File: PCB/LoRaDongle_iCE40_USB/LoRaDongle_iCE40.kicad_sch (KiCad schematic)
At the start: 6 parts, among them J1 USB_A, J2 Conn_01x08

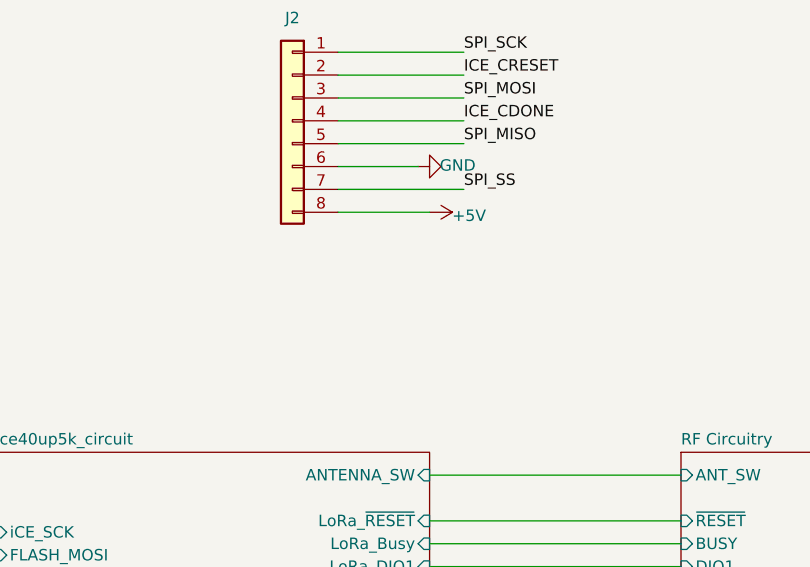
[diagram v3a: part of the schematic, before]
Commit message: updated schematic to QFN ice40
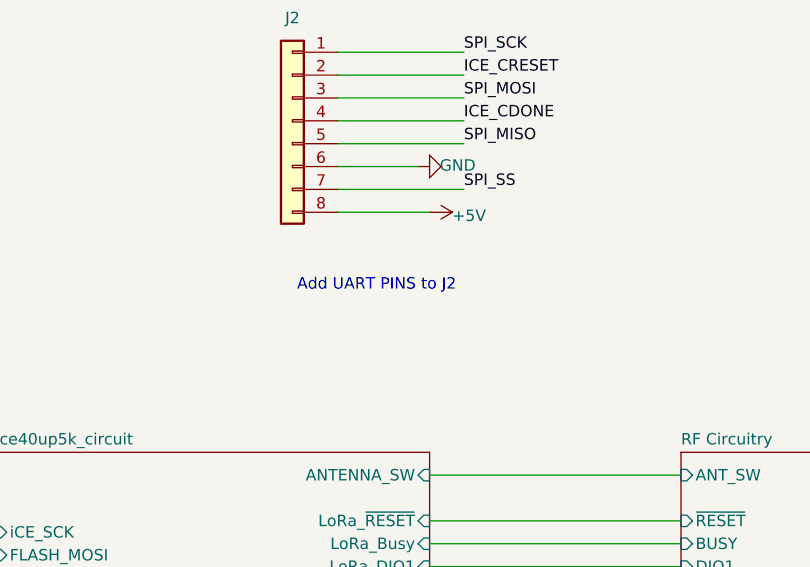
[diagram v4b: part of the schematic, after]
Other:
- note added: "Add UART PINS to J2"
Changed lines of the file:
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@@
     (stroke (width 0) (type default) (color 0 0 0 0))
+  )
+  (text "Add UART PINS to J2" (at 156.718 66.04 0)
+    (effects (font (size 1.27 1.27)) (justify left bottom))
   )
   (text "Configuration Header/Testpoints" (at 149.86 31.75 0)
@@
       (reference "#PWR017") (unit 1) (value "GND") (footprint "")
     )
-    (path "/00000000-0000-0000-0000-0000618d30e5/00000000-0000-0000-0000-000061b1a37c"
-      (reference "#PWR018") (unit 1) (value "GND") (footprint "")
-    )
     (path "/00000000-0000-0000-0000-0000618d30e5/00000000-0000-0000-0000-000061bb6e8b"
       (reference "#PWR019") (unit 1) (value "GND") (footprint "")
@@
       (reference "C55") (unit 1) (value "1uF") (footprint "Capacitor_SMD:C_0402_1005Metric_Pad0.74x0.62mm_HandSolder")
     )
+    (path "/00000000-0000-0000-0000-0000618d30e5/46466808-c3e7-4f98-9aec-1d0c34898718"
+      (reference "C?") (unit 1) (value "100nF") (footprint "Capacitor_SMD:C_0402_1005Metric_Pad0.74x0.62mm_HandSolder")
+    )
+    (path "/00000000-0000-0000-0000-0000618d30e5/798270cd-5a11-4361-915d-f990179c4c4d"
+      (reference "C?") (unit 1) (value "1uF") (footprint "Capacitor_SMD:C_0402_1005Metric_Pad0.74x0.62mm_HandSolder")
+    )
     (path "/00000000-0000-0000-0000-0000614f0720/00000000-0000-0000-0000-000061d45a7d"
       (reference "CTL2") (unit 1) (value "CTL2") (footprint "TestPoint:TestPoint_Pad_D2.5mm")
@@
       (reference "IC1") (unit 1) (value "93LC56BT-I_OT") (footprint "93LC56B-I_OT_KiCad:SOT95P270X145-6N")
     )
-    (path "/00000000-0000-0000-0000-0000618d30e5/00000000-0000-0000-0000-000061af95e0"
-      (reference "IC2") (unit 1) (value "ICE40UP5K-UWG30ITR1K") (footprint "ICE40UP5K-UWG30ITR1K_KiCad:BGA30C40P5X6_211X254X60")
-    )
     (path "/00000000-0000-0000-0000-0000618d30e5/f356286c-5381-4e19-bb6f-5643e839da16"
       (reference "IC3") (unit 1) (value "SGP40-D-R4") (footprint "KiCad_SGP40-D-R4:SON80P244X244X95-7N")
@@
       (reference "J8") (unit 1) (value "Jumper_2_Open") (footprint "Connector_PinHeader_2.54mm:PinHeader_1x02_P2.54mm_Vertical")
     )
+    (path "/00000000-0000-0000-0000-0000618d30e5/ce712167-16e9-4787-a679-59dd7042cff8"
+      (reference "J9") (unit 1) (value "Conn_01x17_Male") (footprint "Connector_PinHeader_2.54mm:PinHeader_1x17_P2.54mm_Vertical")
+    )
     (path "/00000000-0000-0000-0000-0000618d30e5/671729c9-90fa-4cb2-ac5f-b42b2914af94"
       (reference "JP1") (unit 1) (value "SolderJumper_2_Open") (footprint "Resistor_SMD:R_0603_1608Metric_Pad0.98x0.95mm_HandSolder")
@@
       (reference "U5") (unit 1) (value "W25Q128JVS") (footprint "Package_SO:SOIC-8_5.23x5.23mm_P1.27mm")
     )
+    (path "/00000000-0000-0000-0000-0000618d30e5/1ce0333e-6de8-4616-940b-d476ef4ba385"
+      (reference "U6") (unit 1) (value "ICE40UP5K-SG48ITR") (footprint "Package_DFN_QFN:QFN-48-1EP_7x7mm_P0.5mm_EP5.6x5.6mm")
+    )
+    (path "/00000000-0000-0000-0000-0000618d30e5/4ca096aa-df1d-4e7c-9158-2031ee071920"
+      (reference "U6") (unit 2) (value "ICE40UP5K-SG48ITR") (footprint "Package_DFN_QFN:QFN-48-1EP_7x7mm_P0.5mm_EP5.6x5.6mm")
+    )
+    (path "/00000000-0000-0000-0000-0000618d30e5/aec76c06-f2a1-41fa-89c1-1f27b85458b6"
+      (reference "U6") (unit 3) (value "ICE40UP5K-SG48ITR") (footprint "Package_DFN_QFN:QFN-48-1EP_7x7mm_P0.5mm_EP5.6x5.6mm")
+    )
+    (path "/00000000-0000-0000-0000-0000618d30e5/53fb07c9-cb96-4429-a71b-a426d6ac2c63"
+      (reference "U6") (unit 4) (value "ICE40UP5K-SG48ITR") (footprint "Package_DFN_QFN:QFN-48-1EP_7x7mm_P0.5mm_EP5.6x5.6mm")
+    )
     (path "/00000000-0000-0000-0000-0000618d30e5/00000000-0000-0000-0000-000061bb2826"

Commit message: updated routing
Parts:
- removed J2: Conn_01x08, Connector_PinHeader_2.54mm:PinHeader_2x04_P2.54mm_Vertical, symbol Connector_Generic:Conn_01x08
- added J2: Conn_01x10_Male, Connector_PinHeader_2.54mm:PinHeader_2x05_P2.54mm_Vertical, symbol Connector:Conn_01x10_Male
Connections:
- net +5V: now also J2.10 (Pin_10)
- net GND: now also J2.9 (Pin_9)
- net ICE_CDONE: now also J2.4 (Pin_4)
- net ICE_CRESET: now also J2.2 (Pin_2)
- net SPI_MISO: now also J2.5 (Pin_5)
- net SPI_MOSI: now also J2.3 (Pin_3)
- net SPI_SCK: now also J2.1 (Pin_1)
- net SPI_SS: now also J2.6 (Pin_6)
- new net UART_RX: J2.7 (Pin_7)
- new net UART_TX: J2.8 (Pin_8)
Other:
- note removed: "Add UART PINS to J2"
- note removed: "Configuration Header/Testpoints"

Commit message: routing complete
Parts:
- added 5V1: 5V, TestPoint:TestPoint_Pad_D2.5mm, symbol Connector:TestPoint_Flag
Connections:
- net +5V: now also 5V1.1
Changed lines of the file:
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@@
   (junction (at 39.37 92.71) (diameter 0) (color 0 0 0 0)
+  )
+  (junction (at 112.014 40.64) (diameter 0) (color 0 0 0 0)
   )
   (no_connect (at 27.94 107.95))
@@
     (stroke (width 0) (type default) (color 0 0 0 0))
   )
-  (wire (pts (xy 112.014 37.338) (xy 112.014 44.958))
+  (wire (pts (xy 112.014 37.338) (xy 112.014 40.64))
     (stroke (width 0) (type default) (color 0 0 0 0))
   )
@@
   )
   (wire (pts (xy 30.48 107.95) (xy 30.48 110.49))
+    (stroke (width 0) (type default) (color 0 0 0 0))
+  )
+  (wire (pts (xy 112.014 40.64) (xy 112.014 44.958))
     (stroke (width 0) (type default) (color 0 0 0 0))
   )
@@
     )
     (property "Datasheet" "" (id 3) (at 155.956 59.436 0)
+      (effects (font (size 1.27 1.27)) hide)
+    )
+    (pin "1")
+  )
+  (symbol (lib_id "Connector:TestPoint_Flag") (at 112.014 40.64 0) (unit 1)
+    (in_bom yes) (on_board yes)
+    (property "Reference" "5V1" (id 0) (at 119.761 39.4208 0))
+    (property "Value" "5V" (id 1) (at 119.7864 39.4208 90)
+      (effects (font (size 1.27 1.27)) hide)
+    )
+    (property "Footprint" "TestPoint:TestPoint_Pad_D2.5mm" (id 2) (at 117.094 40.64 0)
+      (effects (font (size 1.27 1.27)) hide)
+    )
+    (property "Datasheet" "~" (id 3) (at 117.094 40.64 0)
+      (effects (font (size 1.27 1.27)) hide)
+    )
+    (property "Description" "Test Point" (id 4) (at 112.014 40.64 0)
+      (effects (font (size 1.27 1.27)) hide)
+    )
+    (property "Manufacturer" "-" (id 5) (at 112.014 40.64 0)
+      (effects (font (size 1.27 1.27)) hide)
+    )
+    (property "Manufacturer Part Number" "-" (id 6) (at 112.014 40.64 0)
+      (effects (font (size 1.27 1.27)) hide)
+    )
+    (property "Package" "-" (id 7) (at 112.014 40.64 0)
+      (effects (font (size 1.27 1.27)) hide)
+    )
+    (property "Type" "-" (id 8) (at 112.014 40.64 0)
       (effects (font (size 1.27 1.27)) hide)
     )
@@
       (reference "3V3") (unit 1) (value "3.3V") (footprint "TestPoint:TestPoint_Pad_D2.5mm")
     )
+    (path "/5fa5f0aa-6f4c-4b09-ab26-5eb3ebef5de0"
+      (reference "5V1") (unit 1) (value "5V") (footprint "TestPoint:TestPoint_Pad_D2.5mm")
+    )
     (path "/00000000-0000-0000-0000-000061593dc4"

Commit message: updated BOM
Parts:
- J2: Manufacturer (none) -> -; Manufacturer Part Number (none) -> -; Package (none) -> -
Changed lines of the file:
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@@
+      (effects (font (size 1.27 1.27)) hide)
+    )
+    (property "Description" "2x05 Male Header" (id 4) (at 147.828 49.276 0)
+      (effects (font (size 1.27 1.27)) hide)
+    )
+    (property "Manufacturer" "-" (id 5) (at 147.828 49.276 0)
+      (effects (font (size 1.27 1.27)) hide)
+    )
+    (property "Manufacturer Part Number" "-" (id 6) (at 147.828 49.276 0)
+      (effects (font (size 1.27 1.27)) hide)
+    )
+    (property "Package" "-" (id 7) (at 147.828 49.276 0)
       (effects (font (size 1.27 1.27)) hide)
     )

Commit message: updated silkscreen
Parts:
- J2: Type (none) -> Through HOle
- R1, R2: Type (none) -> SMD
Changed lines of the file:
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@@
+      (effects (font (size 1.27 1.27)) hide)
+    )
+    (property "Type" "SMD" (id 8) (at 50.8 97.79 0)
       (effects (font (size 1.27 1.27)) hide)
     )
@@
       (effects (font (size 1.27 1.27)) hide)
     )
+    (property "Type" "SMD" (id 8) (at 50.8 100.33 0)
+      (effects (font (size 1.27 1.27)) hide)
+    )
     (pin "1")
     (pin "2")
@@
     )
     (property "Package" "-" (id 7) (at 147.828 49.276 0)
+      (effects (font (size 1.27 1.27)) hide)
+    )
+    (property "Type" "Through HOle" (id 8) (at 147.828 49.276 0)
       (effects (font (size 1.27 1.27)) hide)
     )
@@
     )
     (path "/00000000-0000-0000-0000-0000618d30e5/1ce0333e-6de8-4616-940b-d476ef4ba385"
-      (reference "U6") (unit 1) (value "ICE40UP5K-SG48ITR") (footprint "Package_DFN_QFN:QFN-48-1EP_7x7mm_P0.5mm_EP5.6x5.6mm")
+      (reference "U6") (unit 1) (value "ICE40UP5K-SG48I") (footprint "Package_DFN_QFN:QFN-48-1EP_7x7mm_P0.5mm_EP5.6x5.6mm")
     )
     (path "/00000000-0000-0000-0000-0000618d30e5/4ca096aa-df1d-4e7c-9158-2031ee071920"
-      (reference "U6") (unit 2) (value "ICE40UP5K-SG48ITR") (footprint "Package_DFN_QFN:QFN-48-1EP_7x7mm_P0.5mm_EP5.6x5.6mm")
+      (reference "U6") (unit 2) (value "ICE40UP5K-SG48I") (footprint "Package_DFN_QFN:QFN-48-1EP_7x7mm_P0.5mm_EP5.6x5.6mm")
     )
     (path "/00000000-0000-0000-0000-0000618d30e5/aec76c06-f2a1-41fa-89c1-1f27b85458b6"
-      (reference "U6") (unit 3) (value "ICE40UP5K-SG48ITR") (footprint "Package_DFN_QFN:QFN-48-1EP_7x7mm_P0.5mm_EP5.6x5.6mm")
+      (reference "U6") (unit 3) (value "ICE40UP5K-SG48I") (footprint "Package_DFN_QFN:QFN-48-1EP_7x7mm_P0.5mm_EP5.6x5.6mm")
     )
     (path "/00000000-0000-0000-0000-0000618d30e5/53fb07c9-cb96-4429-a71b-a426d6ac2c63"
-      (reference "U6") (unit 4) (value "ICE40UP5K-SG48ITR") (footprint "Package_DFN_QFN:QFN-48-1EP_7x7mm_P0.5mm_EP5.6x5.6mm")
+      (reference "U6") (unit 4) (value "ICE40UP5K-SG48I") (footprint "Package_DFN_QFN:QFN-48-1EP_7x7mm_P0.5mm_EP5.6x5.6mm")
     )
     (path "/00000000-0000-0000-0000-0000618d30e5/00000000-0000-0000-0000-000061bb2826"
